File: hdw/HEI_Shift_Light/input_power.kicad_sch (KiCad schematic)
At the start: 16 parts, among them J201 VIN, U201 TPS26624DRCR

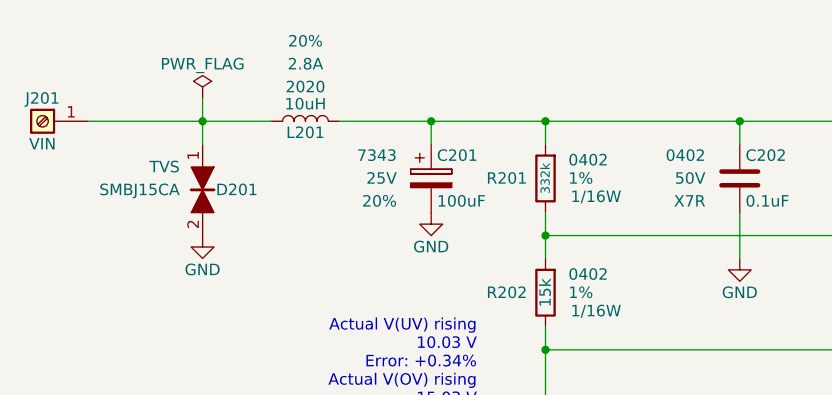
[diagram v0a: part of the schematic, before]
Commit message: added stackup, design rules
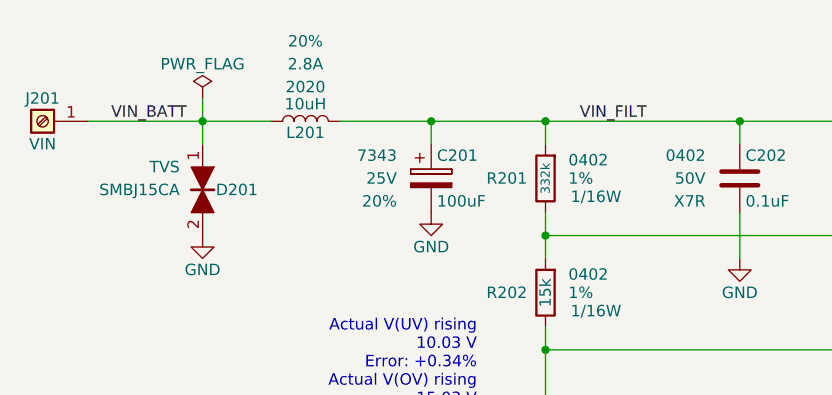
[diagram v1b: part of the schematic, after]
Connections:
- net VIN_BATT: now reaches D201.1, J201.1 (Pin_1), L201.1
- net VIN_FILT: now reaches C201.1, C202.1, L201.2, R201.1, U201.1 (IN)
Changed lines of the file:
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@@
+		)
+	)
+	(label "VIN_BATT"
+		(at 49.53 49.53 0)
+		(effects
+			(font
+				(size 1.27 1.27)
+			)
+			(justify left bottom)
+		)
+	)
+	(label "VIN_FILT"
+		(at 101.6 49.53 0)
+		(effects
+			(font
+				(size 1.27 1.27)
+			)
+			(justify left bottom)
 		)
 	)
